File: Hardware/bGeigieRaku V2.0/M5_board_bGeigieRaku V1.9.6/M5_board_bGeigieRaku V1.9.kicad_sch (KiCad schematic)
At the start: 23 parts, among them J1 M5 2x15 pin, J10 QI GND, J11 QI charger Plus, J2 Geiger, J3 GPS, J7 Conn_01x14_Female, J8 QI charger GND, J9 QI Plus, Q1 IRF4905, Q2 IRF4905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

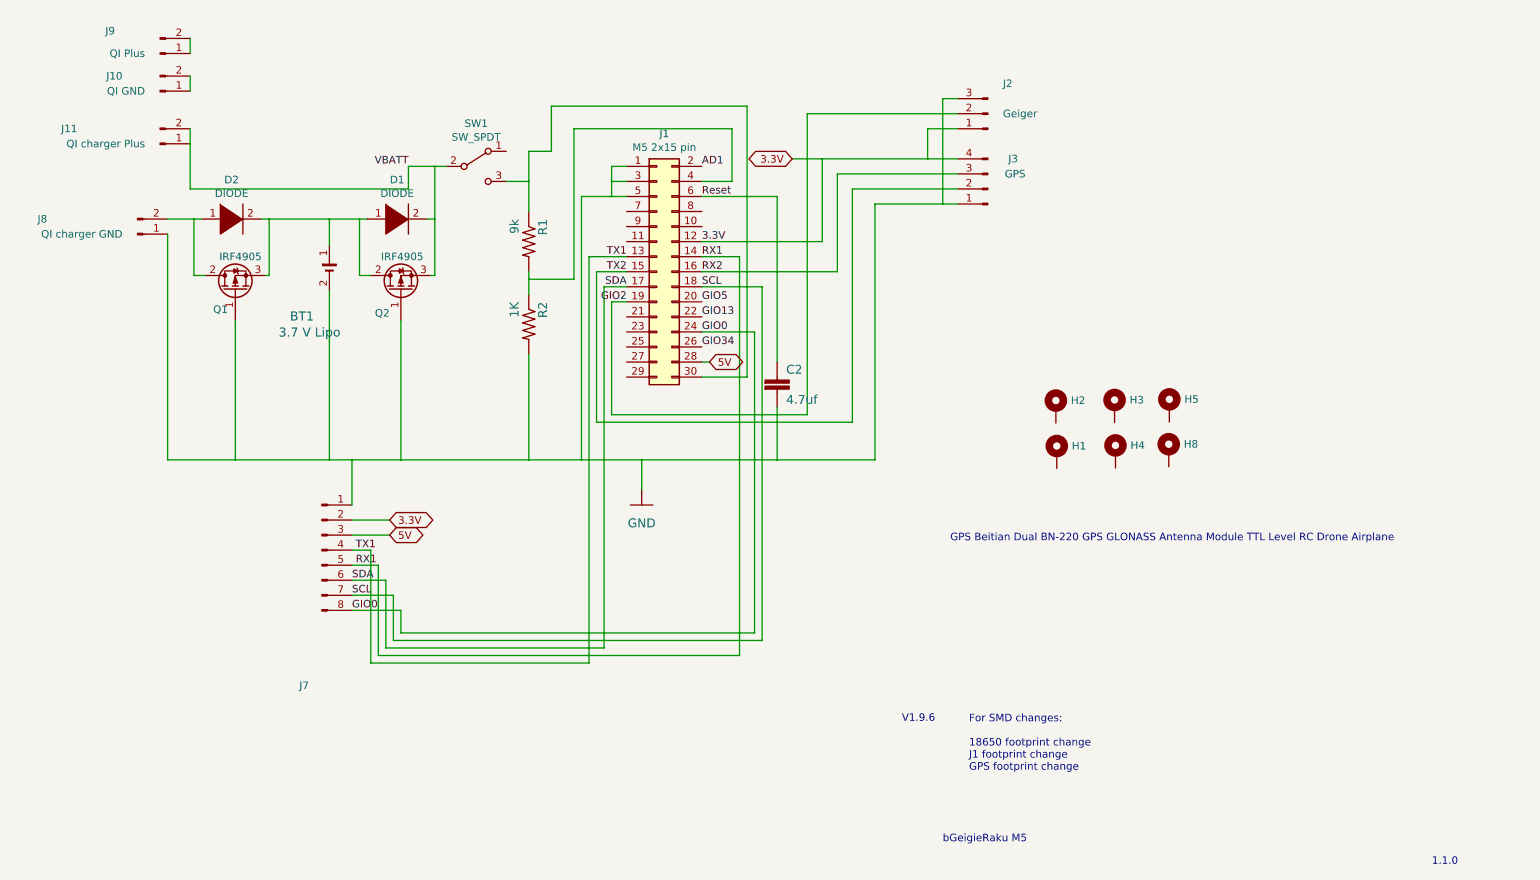
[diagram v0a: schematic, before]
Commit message: Made changes on board after new V1.9.6 came back
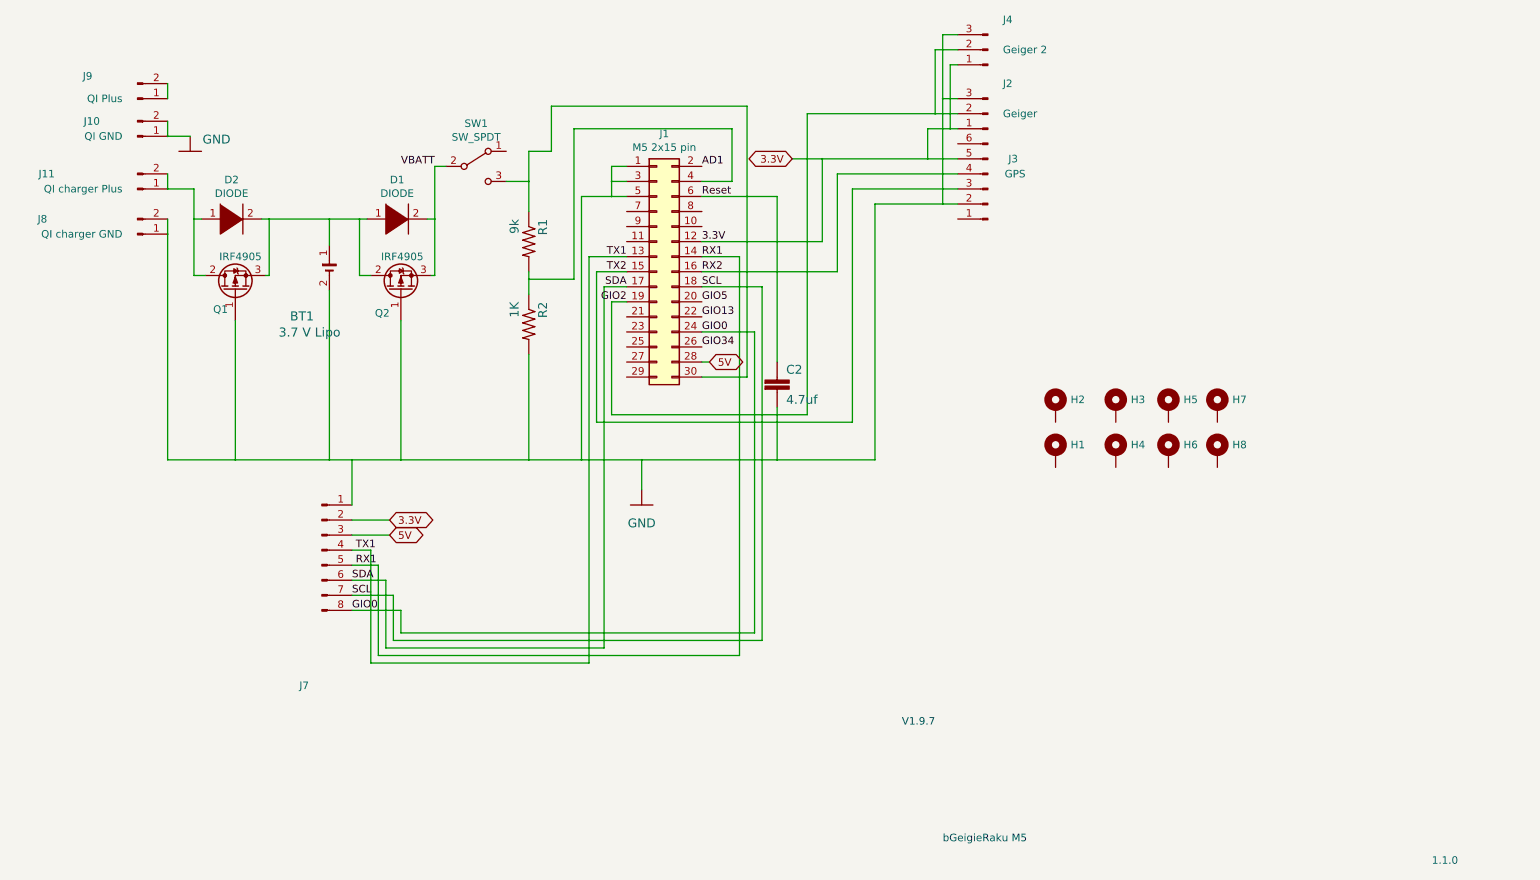
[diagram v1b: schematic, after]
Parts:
- added H6, H7: MountingHole_Pad, MountingHole:MountingHole_3.2mm_M3, symbol Mechanical:MountingHole_Pad
- added J4: Geiger 2, Connector_PinHeader_2.54mm:PinHeader_1x03_P2.54mm_Vertical, symbol Connector:Conn_01x03_Male
- J3: footprint Connector_PinSocket_2.54mm:PinSocket_1x04_P2.54mm_Vertical -> Connector_PinSocket_2.54mm:PinSocket_1x06_P2.54mm_Vertical; symbol Connector:Conn_01x04_Male -> Connector:Conn_01x06_Male
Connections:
- net 3.3V: now also J3.5 (Pin_5), J4.1 (Pin_1); no longer J3.4 (Pin_4)
- net GIO2: now also J4.2 (Pin_2)
- net GND: now also J10.1 (Pin_1), J10.2 (Pin_2), J3.2 (Pin_2), J8.2 (Pin_2), J4.3 (Pin_3); no longer J3.1 (Pin_1)
- net RX2: now also J3.4 (Pin_4); no longer J3.3 (Pin_3)
- net TX2: now also J3.3 (Pin_3); no longer J3.2 (Pin_2)
- net VBATT: no longer J11.1 (Pin_1), J11.2 (Pin_2)
- net at D2.1 (K), Q1.2 (D): now also J11.1 (Pin_1), J11.2 (Pin_2); no longer J8.2 (Pin_2)
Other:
- note added: "V1.9.7"
- note removed: "For SMD changes: 18650 footprint change J1 footprint change GPS footprint change"
- note removed: "GPS Beitian Dual BN-220 GPS GLONASS Antenna Module TTL Level RC Drone Airplane"
- note removed: "V1.9.6"
- moved on the sheet: H8, J10, J11, J9

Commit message: Mirrored pins of M5connector, used smaller diodes.
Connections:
- net 3.3V: now also J1.11 (Pin_11); no longer J1.12 (Pin_12)
- net 5V: now also J1.27 (Pin_27); no longer J1.28 (Pin_28)
- net AD1: now also J1.1 (Pin_1); no longer J1.2 (Pin_2)
- net GIO0: now also J1.23 (Pin_23); no longer J1.24 (Pin_24)
- net GIO13: now also J1.21 (Pin_21); no longer J1.22 (Pin_22)
- net GIO2: now also J1.20 (Pin_20); no longer J1.19 (Pin_19)
- net GIO34: now also J1.25 (Pin_25); no longer J1.26 (Pin_26)
- net GIO5: now also J1.19 (Pin_19); no longer J1.20 (Pin_20)
- net GND: now also J1.2 (Pin_2), J1.4 (Pin_4), J1.6 (Pin_6); no longer J1.1 (Pin_1), J1.3 (Pin_3), J1.5 (Pin_5)
- net RX1: now also J1.13 (Pin_13); no longer J1.14 (Pin_14)
- net RX2: now also J1.15 (Pin_15); no longer J1.16 (Pin_16)
- net Reset: now also J1.5 (Pin_5); no longer J1.6 (Pin_6)
- net SCL: now also J1.17 (Pin_17); no longer J1.18 (Pin_18)
- net SDA: now also J1.18 (Pin_18); no longer J1.17 (Pin_17)
- net TX1: now also J1.14 (Pin_14); no longer J1.13 (Pin_13)
- net TX2: now also J1.16 (Pin_16); no longer J1.15 (Pin_15)
- net at J1.29 (Pin_29): now also R1.1, SW1.3 (C)
- net at R1.2, R2.1: now also J1.3 (Pin_3); no longer J1.4 (Pin_4)
- now unconnected: J1.30 (Pin_30)
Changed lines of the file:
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@@
     (pin "3")
   )
-  (symbol (lib_id "Connector_Generic:Conn_02x15_Odd_Even") (at 138.43 93.98 0) (unit 1)
+  (symbol (lib_id "Connector_Generic:Conn_02x15_Odd_Even") (at 140.97 93.98 0) (mirror y) (unit 1)
     (in_bom yes) (on_board yes)
     (property "Reference" "J1" (id 0) (at 139.7 70.6882 0))
     (property "Value" "M5 2x15 pin" (id 1) (at 139.7 72.9996 0))
-    (property "Footprint" "Connector_PinHeader_2.54mm:PinHeader_2x15_P2.54mm_Vertical_SMD" (id 2) (at 138.43 93.98 0)
+    (property "Footprint" "Connector_PinHeader_2.54mm:PinHeader_2x15_P2.54mm_Vertical_SMD" (id 2) (at 140.97 93.98 0)
       (effects (font (size 1.27 1.27)) hide)
     )
-    (property "Datasheet" "~" (id 3) (at 138.43 93.98 0)
+    (property "Datasheet" "~" (id 3) (at 140.97 93.98 0)
       (effects (font (size 1.27 1.27)) hide)
     )
